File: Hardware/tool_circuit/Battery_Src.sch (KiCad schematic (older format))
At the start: 1 part

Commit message: schematic revisions
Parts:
- gave numbers to parts that had none: 1
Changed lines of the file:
@@
 $EndComp
 $Comp
-L EJ503A:EJ503A J?
+L EJ503A:EJ503A J1
 U 1 1 614F5D56
 P 4750 3500
-F 0 "J?" H 4732 3805 50  0000 C CNN
+F 0 "J1" H 4732 3805 50  0000 C CNN
 F 1 "EJ503A" H 4732 3714 50  0000 C CNN
 F 2 "MPD_EJ503A" H 4750 3500 50  0001 L BNN

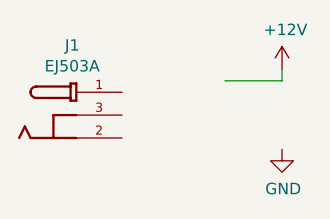
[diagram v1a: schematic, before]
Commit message: schematic LEDs + switch
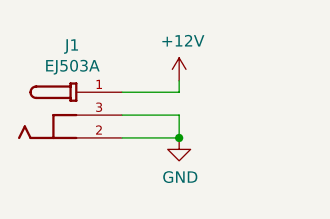
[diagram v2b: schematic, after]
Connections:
- wire segments 2 -> 5
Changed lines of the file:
@@
 L power:+12V #PWR04
 U 1 1 614E4DBC
-P 5650 3300
-F 0 "#PWR04" H 5650 3150 50  0001 C CNN
-F 1 "+12V" H 5665 3473 50  0000 C CNN
-F 2 "" H 5650 3300 50  0001 C CNN
-F 3 "" H 5650 3300 50  0001 C CNN
-	1    5650 3300
+P 5200 3350
+F 0 "#PWR04" H 5200 3200 50  0001 C CNN
+F 1 "+12V" H 5215 3523 50  0000 C CNN
+F 2 "" H 5200 3350 50  0001 C CNN
+F 3 "" H 5200 3350 50  0001 C CNN
+	1    5200 3350
 	1    0    0    -1
 $EndComp
@@
 L power:GND #PWR05
 U 1 1 614E58F8
-P 5650 3650
-F 0 "#PWR05" H 5650 3400 50  0001 C CNN
-F 1 "GND" H 5655 3477 50  0000 C CNN
-F 2 "" H 5650 3650 50  0001 C CNN
-F 3 "" H 5650 3650 50  0001 C CNN
-	1    5650 3650
+P 5200 3600
+F 0 "#PWR05" H 5200 3350 50  0001 C CNN
+F 1 "GND" H 5205 3427 50  0000 C CNN
+F 2 "" H 5200 3600 50  0001 C CNN
+F 3 "" H 5200 3600 50  0001 C CNN
+	1    5200 3600
 	1    0    0    -1
 $EndComp
@@
 $EndComp
 Wire Wire Line
-	5650 3300 5650 3350
+	5200 3350 5200 3400
 Wire Wire Line
-	5650 3350 5400 3350
+	5200 3400 4950 3400
+Wire Wire Line
+	4950 3500 5200 3500
+Wire Wire Line
+	5200 3500 5200 3600
+Wire Wire Line
+	4950 3600 5200 3600
+Connection ~ 5200 3600
 $EndSCHEMATC

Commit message: PCB changes
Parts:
- J1: footprint MPD_EJ503A -> EJ503A:MPD_EJ503A
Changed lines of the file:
@@
 F 0 "J1" H 4732 3805 50  0000 C CNN
 F 1 "EJ503A" H 4732 3714 50  0000 C CNN
-F 2 "MPD_EJ503A" H 4750 3500 50  0001 L BNN
+F 2 "EJ503A:MPD_EJ503A" H 4750 3500 50  0001 L BNN
 F 3 "" H 4750 3500 50  0001 L BNN
 F 4 "11 mm" H 4750 3500 50  0001 L BNN "MAXIMUM_PACKAGE_HEIGHT"

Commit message: pcb
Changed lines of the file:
@@
 	5200 3350 5200 3400
 Wire Wire Line
-	5200 3400 4950 3400
+	5200 3400 5050 3400
 Wire Wire Line
 	4950 3500 5200 3500
@@
 	4950 3600 5200 3600
 Connection ~ 5200 3600
+$Comp
+L power:PWR_FLAG #FLG02
+U 1 1 61A59848
+P 5050 3400
+F 0 "#FLG02" H 5050 3475 50  0001 C CNN
+F 1 "PWR_FLAG" H 5050 3573 50  0000 C CNN
+F 2 "" H 5050 3400 50  0001 C CNN
+F 3 "~" H 5050 3400 50  0001 C CNN
+	1    5050 3400
+	1    0    0    -1
+$EndComp
+Connection ~ 5050 3400
+Wire Wire Line
+	5050 3400 4950 3400
 $EndSCHEMATC
